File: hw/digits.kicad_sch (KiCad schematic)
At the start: 49 parts, among them J11 Conn_02x09_Odd_Even, J12 Conn_02x09_Odd_Even, J13 Conn_02x09_Odd_Even

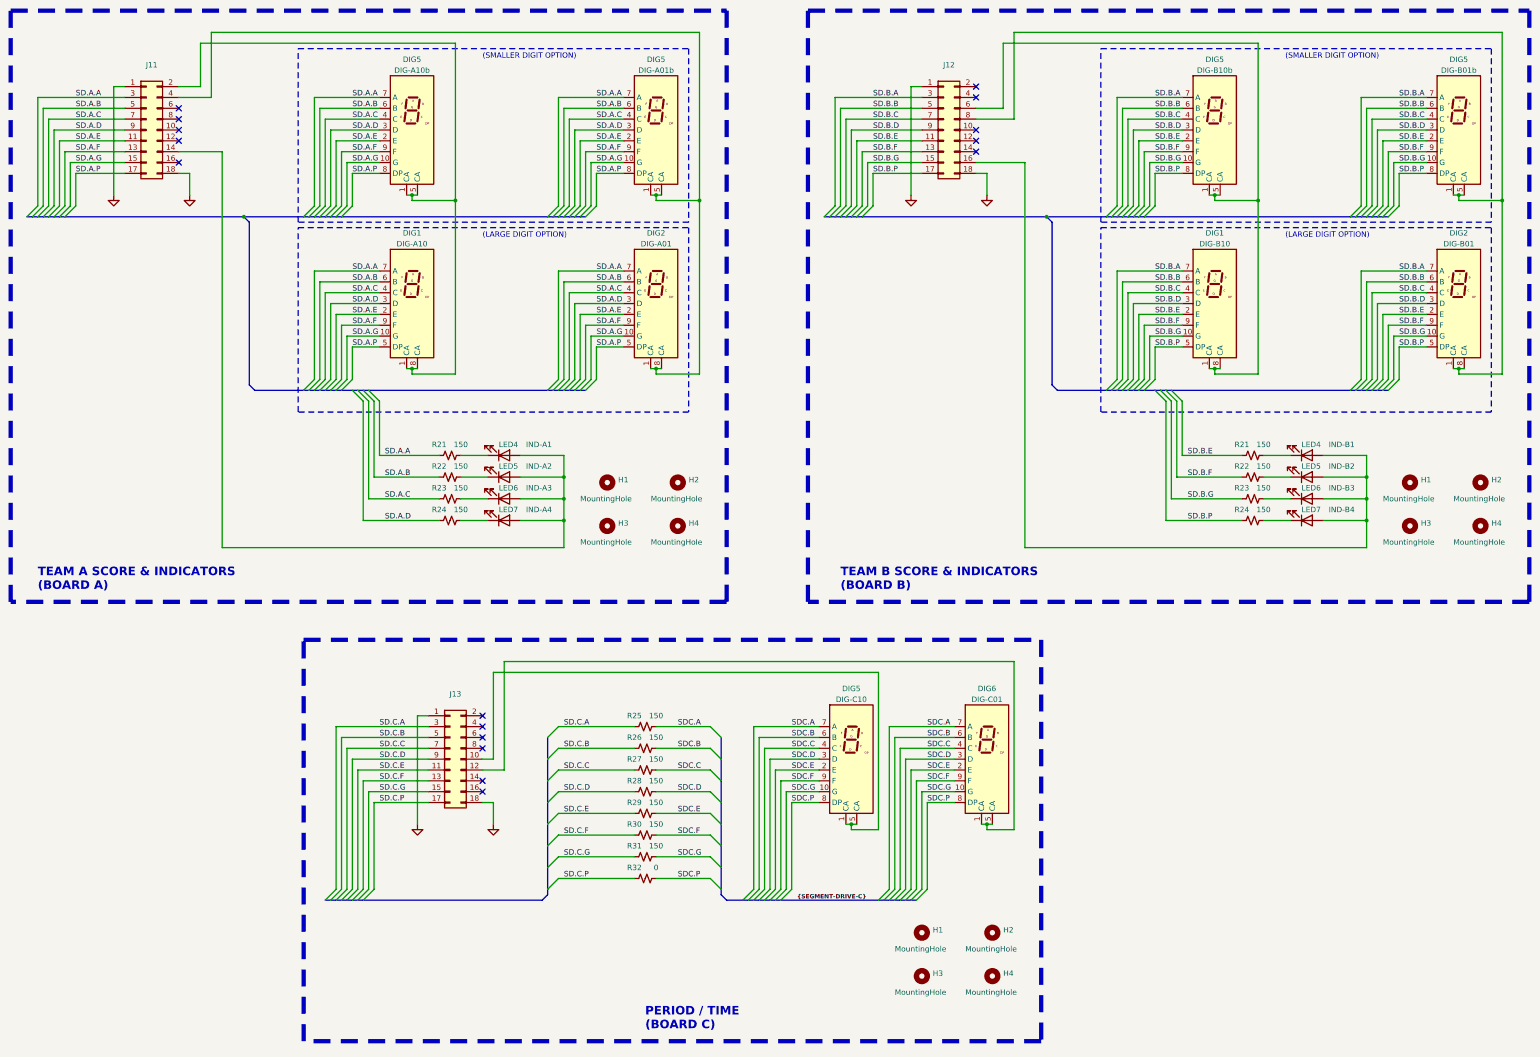
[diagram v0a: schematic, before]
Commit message: Schematic updated with digit drive resistors
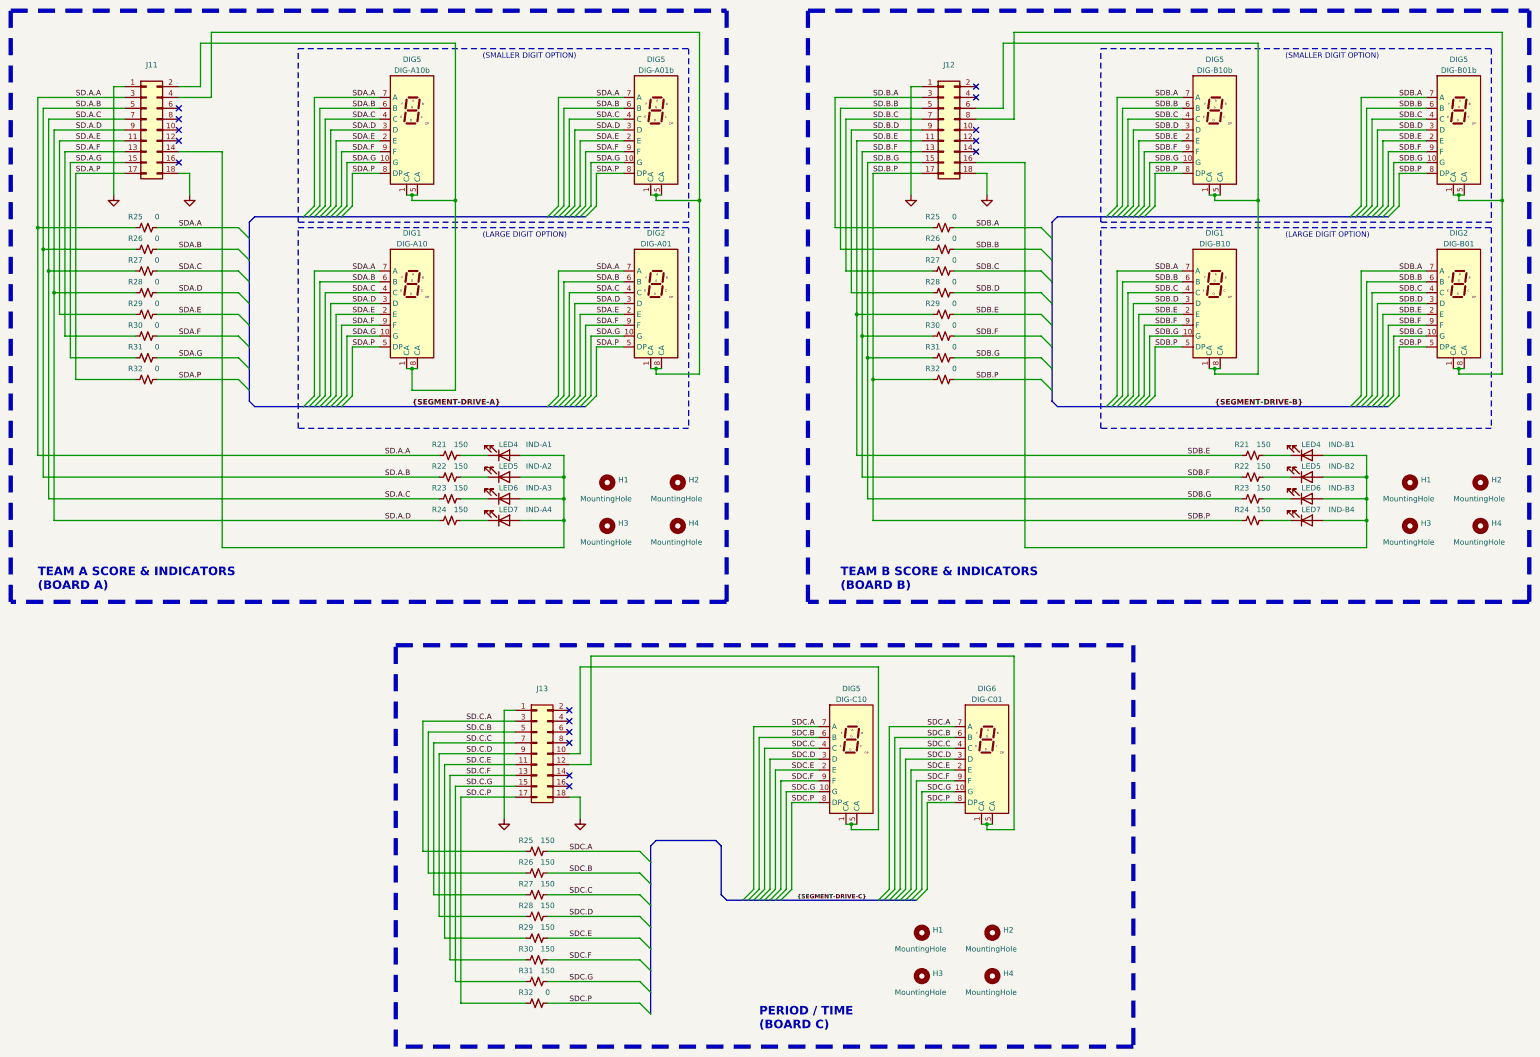
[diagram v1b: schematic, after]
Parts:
- added R25 (x2), R26 (x2), R27 (x2), R28 (x2), R29 (x2), R30 (x2), R31 (x2), R32 (x2): 0, symbol Device:R_Small_US
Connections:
- net SD.A.A: now also R25.1; no longer DIG1.7 (A), DIG2.7 (A), DIG5.7 (A), DIG5.7 (A)
- net SD.A.B: now also R26.1; no longer DIG1.6 (B), DIG2.6 (B), DIG5.6 (B), DIG5.6 (B)
- net SD.A.C: now also R27.1; no longer DIG1.4 (C), DIG2.4 (C), DIG5.4 (C), DIG5.4 (C)
- net SD.A.D: now also R28.1; no longer DIG1.3 (D), DIG2.3 (D), DIG5.3 (D), DIG5.3 (D)
- net SD.A.E: now also R29.1; no longer DIG1.2 (E), DIG2.2 (E), DIG5.2 (E), DIG5.2 (E)
- net SD.A.F: now also R30.1; no longer DIG1.9 (F), DIG2.9 (F), DIG5.9 (F), DIG5.9 (F)
- net SD.A.G: now also R31.1; no longer DIG1.10 (G), DIG2.10 (G), DIG5.10 (G), DIG5.10 (G)
- net SD.A.P: now also R32.1; no longer DIG1.5 (DP), DIG2.5 (DP), DIG5.8 (DP), DIG5.8 (DP)
- net SD.B.A: now also R25.1; no longer DIG1.7 (A), DIG2.7 (A), DIG5.7 (A), DIG5.7 (A)
- net SD.B.B: now also R26.1; no longer DIG1.6 (B), DIG2.6 (B), DIG5.6 (B), DIG5.6 (B)
- net SD.B.C: now also R27.1; no longer DIG1.4 (C), DIG2.4 (C), DIG5.4 (C), DIG5.4 (C)
- net SD.B.D: now also R28.1; no longer DIG1.3 (D), DIG2.3 (D), DIG5.3 (D), DIG5.3 (D)
- net SD.B.E: now also R29.1, R29.2
- net SD.B.F: now also R30.1, R30.2
- net SD.B.G: now also R31.1, R31.2
- net SD.B.P: now also R32.1, R32.2
- new net SDA.A: DIG1.7 (A), DIG2.7 (A), DIG5.7 (A), DIG5.7 (A), R25.2
- new net SDA.B: DIG1.6 (B), DIG2.6 (B), DIG5.6 (B), DIG5.6 (B), R26.2
- new net SDA.C: DIG1.4 (C), DIG2.4 (C), DIG5.4 (C), DIG5.4 (C), R27.2
- new net SDA.D: DIG1.3 (D), DIG2.3 (D), DIG5.3 (D), DIG5.3 (D), R28.2
- new net SDA.E: DIG1.2 (E), DIG2.2 (E), DIG5.2 (E), DIG5.2 (E), R29.2
- new net SDA.F: DIG1.9 (F), DIG2.9 (F), DIG5.9 (F), DIG5.9 (F), R30.2
- new net SDA.G: DIG1.10 (G), DIG2.10 (G), DIG5.10 (G), DIG5.10 (G), R31.2
- new net SDA.P: DIG1.5 (DP), DIG2.5 (DP), DIG5.8 (DP), DIG5.8 (DP), R32.2
- new net SDB.A: DIG1.7 (A), DIG2.7 (A), DIG5.7 (A), DIG5.7 (A), R25.2
- new net SDB.B: DIG1.6 (B), DIG2.6 (B), DIG5.6 (B), DIG5.6 (B), R26.2
- new net SDB.C: DIG1.4 (C), DIG2.4 (C), DIG5.4 (C), DIG5.4 (C), R27.2
- new net SDB.D: DIG1.3 (D), DIG2.3 (D), DIG5.3 (D), DIG5.3 (D), R28.2
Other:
- moved on the sheet: J13, R25, R26, R27, R28, R29, R30, R31, R32

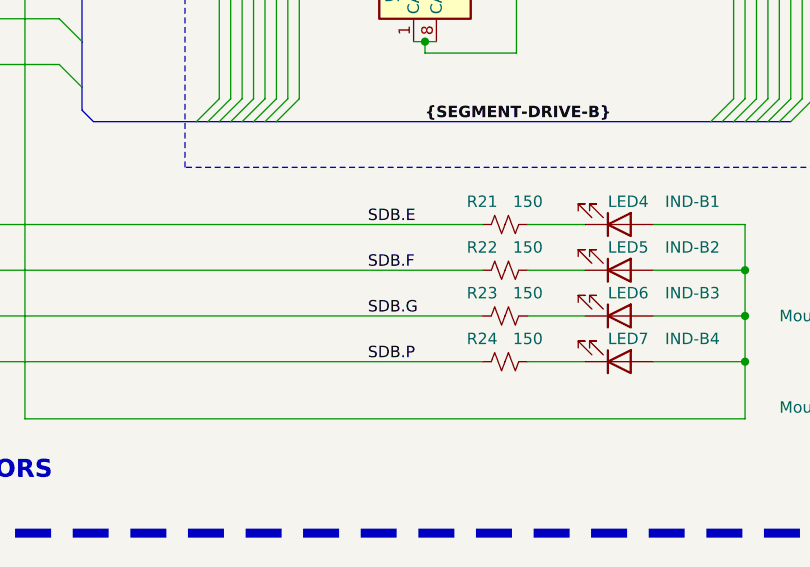
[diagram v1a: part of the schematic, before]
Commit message: Footprints assigned
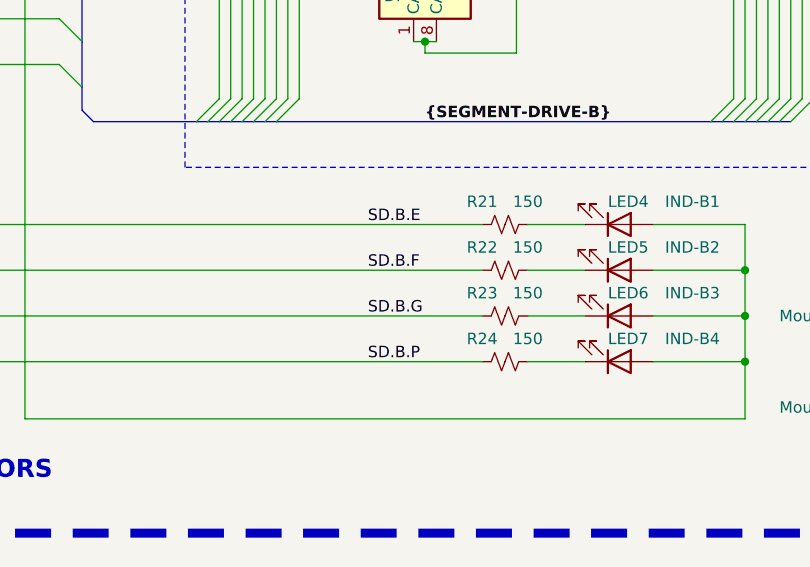
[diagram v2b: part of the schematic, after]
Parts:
- J11, J12, J13: footprint (none) -> Connector_PinHeader_2.54mm:PinHeader_2x09_P2.54mm_Vertical
- LED4, LED5, LED6, LED7: footprint (none) -> LED_THT:LED_D5.0mm-3
- R21, R22, R23, R24, R25, R26, R27, R28, R29, R30, R31, R32: footprint (none) -> Resistor_THT:R_Axial_DIN0207_L6.3mm_D2.5mm_P10.16mm_Horizontal
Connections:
- net SD.B.E: no longer DIG1.2 (E), DIG2.2 (E), DIG5.2 (E), DIG5.2 (E), R29.2
- net SD.B.F: no longer DIG1.9 (F), DIG2.9 (F), DIG5.9 (F), DIG5.9 (F), R30.2
- net SD.B.G: no longer DIG1.10 (G), DIG2.10 (G), DIG5.10 (G), DIG5.10 (G), R31.2
- net SD.B.P: no longer DIG1.5 (DP), DIG2.5 (DP), DIG5.8 (DP), DIG5.8 (DP), R32.2
- new net SDB.E: DIG1.2 (E), DIG2.2 (E), DIG5.2 (E), DIG5.2 (E), R29.2
- new net SDB.F: DIG1.9 (F), DIG2.9 (F), DIG5.9 (F), DIG5.9 (F), R30.2
- new net SDB.G: DIG1.10 (G), DIG2.10 (G), DIG5.10 (G), DIG5.10 (G), R31.2
- new net SDB.P: DIG1.5 (DP), DIG2.5 (DP), DIG5.8 (DP), DIG5.8 (DP), R32.2
